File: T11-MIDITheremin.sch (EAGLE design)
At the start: 102 parts, among them IC1 TL072P, IC2 TL072P, T1 2N3904, T2 2N3904, T3 2N3904, T4 2N3904, T5 2N3904

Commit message: Add files via upload
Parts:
- removed L4, L5, L6: 10mH, rcl:L-US6000-XXX-RC
- added C32: 2200pF, resistor:C-EU050-025X075
- C2, C4: value 3n3 .1% -> 1.2nF
- L1: value 100uH .1% -> 2.5mH; device rcl:L-US6000-XXX-RC -> resistor:L-US0207/5V
- L2: value 100uH .1% -> 100uH; device rcl:L-US6000-XXX-RC -> resistor:L-US0207/5V
- L3: value 10mH -> 100uH; device rcl:L-US6000-XXX-RC -> resistor:L-US0207/5V
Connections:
- removed net ANT: ANT1.1, L6.2
- removed net N$19: L5.1, L6.1
- removed net N$35: L4.2, L5.2
- net N$20: now also C32.1
- net N$28: now also ANT1.1, L1.1; no longer L3.1, L4.1
- net P_OSC_V+: now also L3.1; no longer L1.1
- net V-: now also C32.2
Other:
- moved on the sheet: ANT1, C27, L1, L3, R32, VOUT

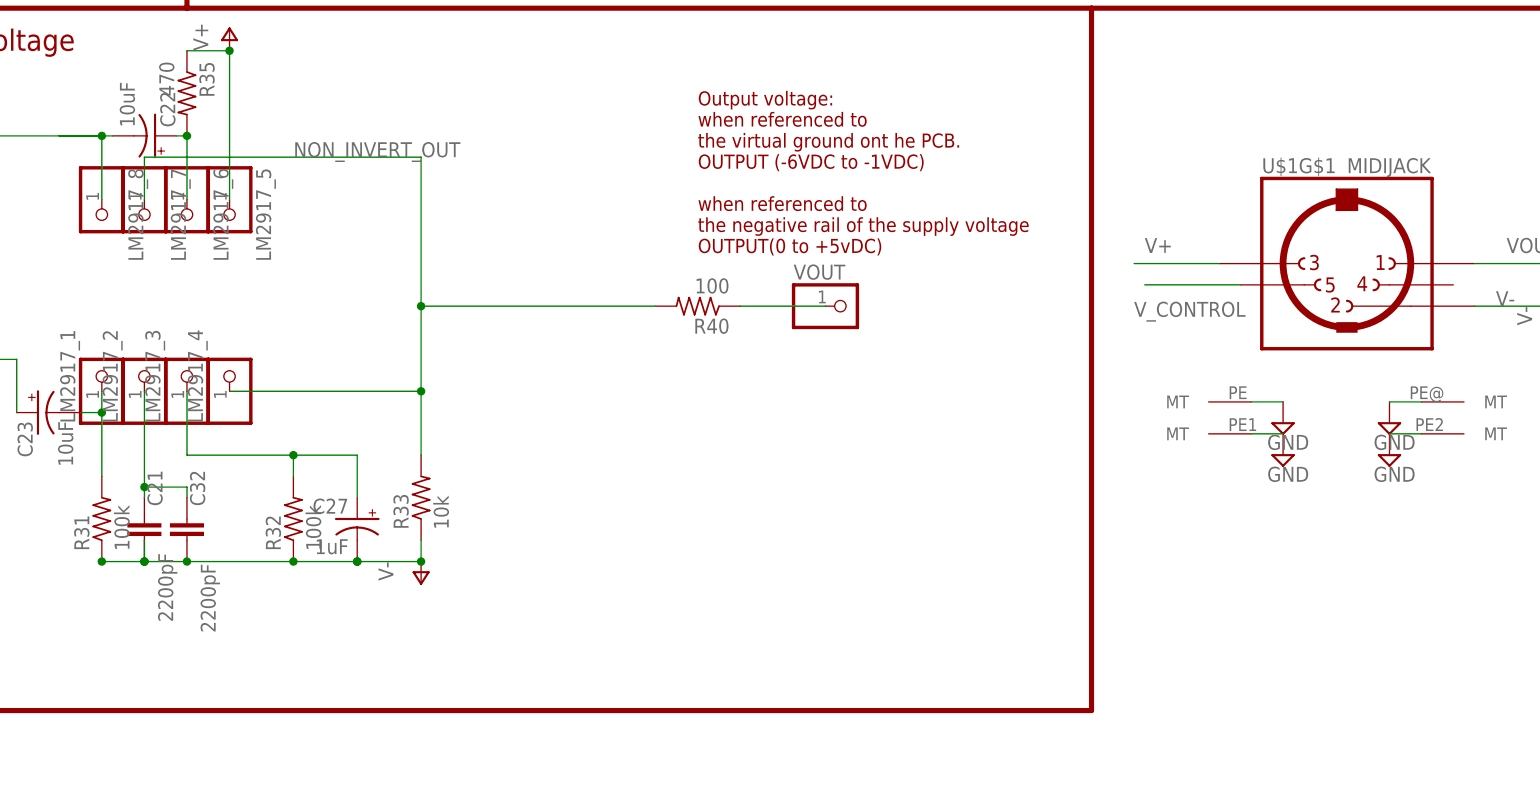
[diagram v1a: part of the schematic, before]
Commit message: fixed some of the silkscreen layer
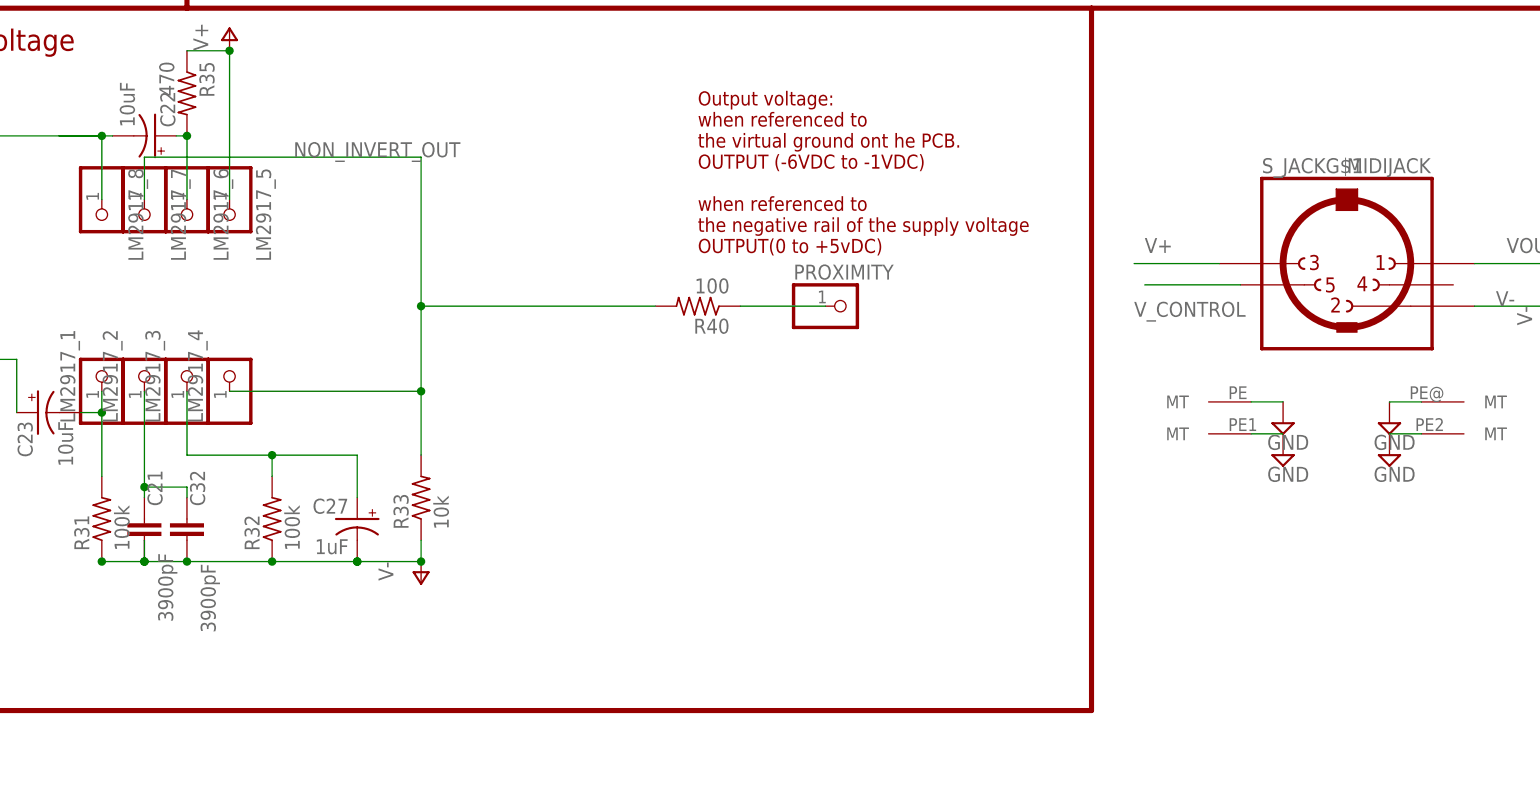
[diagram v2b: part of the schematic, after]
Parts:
- C21, C32: value 2200pF -> 3900pF
- renumbered U$1 to S_JACK, VOUT to PROXIMITY
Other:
- moved on the sheet: R32
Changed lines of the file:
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@@
 <setting verticaltext="up"/>
 </settings>
-<grid distance="0.05" unitdist="inch" unit="inch" style="lines" multiple="1" display="no" altdistance="0.01" altunitdist="inch" altunit="inch"/>
+<grid distance="0.1" unitdist="inch" unit="inch" style="lines" multiple="1" display="no" altdistance="0.01" altunitdist="inch" altunit="inch"/>
 <layers>
 <layer number="1" name="Top" color="4" fill="1" visible="no" active="no"/>
@@
 <part name="P+3" library="supply1" deviceset="V+" device=""/>
 <part name="P-2" library="supply1" deviceset="V-" device=""/>
-<part name="C21" library="resistor" deviceset="C-EU" device="050-025X075" value="2200pF"/>
+<part name="C21" library="resistor" deviceset="C-EU" device="050-025X075" value="3900pF"/>
 <part name="R31" library="rcl" deviceset="R-US_" device="0411/3V" value="100k"/>
 <part name="R32" library="rcl" deviceset="R-US_" device="0411/3V" value="100k"/>
@@
 <part name="LM2917_7" library="pinhead" deviceset="PINHD-1X1" device=""/>
 <part name="LM2917_8" library="pinhead" deviceset="PINHD-1X1" device=""/>
-<part name="VOUT" library="pinhead" deviceset="PINHD-1X1" device=""/>
+<part name="PROXIMITY" library="pinhead" deviceset="PINHD-1X1" device=""/>
 <part name="C27" library="resistor" deviceset="CPOL-US" device="E2.5-7" value="1uF"/>
 <part name="C23" library="resistor" deviceset="CPOL-US" device="E2.5-7" value="10uF"/>
@@
 <part name="C30" library="resistor" deviceset="C-EU" device="050-025X075" value="tune"/>
 <part name="C31" library="resistor" deviceset="C-EU" device="050-025X075" value="tune"/>
-<part name="U$1" library="adafruit" deviceset="MIDIJACK" device=""/>
+<part name="S_JACK" library="adafruit" deviceset="MIDIJACK" device=""/>
 <part name="P-1" library="supply1" deviceset="V-" device=""/>
 <part name="SUPPLY22" library="supply2" deviceset="GND" device=""/>
@@
 <part name="SUPPLY24" library="supply2" deviceset="GND" device=""/>
 <part name="SUPPLY25" library="supply2" deviceset="GND" device=""/>
-<part name="C32" library="resistor" deviceset="C-EU" device="050-025X075" value="2200pF"/>
+<part name="C32" library="resistor" deviceset="C-EU" device="050-025X075" value="3900pF"/>
 <part name="L3" library="resistor" deviceset="L-US" device="0207/5V" value="100uH"/>
 <part name="L1" library="resistor" deviceset="L-US" device="0207/5V" value="2.5mH"/>
@@
 </instance>
 <instance part="R31" gate="G$1" x="208.28" y="106.68" rot="R90"/>
-<instance part="R32" gate="G$1" x="231.14" y="106.68" rot="R90"/>
+<instance part="R32" gate="G$1" x="228.6" y="106.68" rot="R90"/>
 <instance part="R33" gate="G$1" x="246.38" y="109.22" rot="R90"/>
 <instance part="R35" gate="G$1" x="218.44" y="157.48" rot="R270"/>
@@
 <instance part="LM2917_7" gate="G$1" x="213.36" y="142.24" rot="R270"/>
 <instance part="LM2917_8" gate="G$1" x="208.28" y="142.24" rot="R270"/>
-<instance part="VOUT" gate="G$1" x="297.18" y="132.08"/>
+<instance part="PROXIMITY" gate="G$1" x="297.18" y="132.08"/>
 <instance part="C27" gate="G$1" x="238.76" y="106.68" rot="MR0"/>
 <instance part="C23" gate="G$1" x="200.66" y="119.38" rot="MR270"/>
@@
 <instance part="C30" gate="G$1" x="85.09" y="209.55"/>
 <instance part="C31" gate="G$1" x="78.74" y="215.9"/>
-<instance part="U$1" gate="G$1" x="356.87" y="137.16"/>
+<instance part="S_JACK" gate="G$1" x="356.87" y="137.16"/>
 <instance part="P-1" gate="1" x="382.27" y="129.54"/>
-<instance part="U$1" gate="G$2" x="345.44" y="120.65" rot="R180"/>
-<instance part="U$1" gate="G$3" x="365.76" y="120.65"/>
-<instance part="U$1" gate="G$4" x="345.44" y="116.84" rot="R180"/>
-<instance part="U$1" gate="G$5" x="365.76" y="116.84"/>
+<instance part="S_JACK" gate="G$2" x="345.44" y="120.65" rot="R180"/>
+<instance part="S_JACK" gate="G$3" x="365.76" y="120.65"/>
+<instance part="S_JACK" gate="G$4" x="345.44" y="116.84" rot="R180"/>
+<instance part="S_JACK" gate="G$5" x="365.76" y="116.84"/>
 <instance part="SUPPLY22" gate="GND" x="361.95" y="114.3"/>
 <instance part="SUPPLY23" gate="GND" x="349.25" y="114.3"/>
@@
 </segment>
 <segment>
-<pinref part="U$1" gate="G$1" pin="3"/>
+<pinref part="S_JACK" gate="G$1" pin="3"/>
 <wire x1="341.63" y1="137.16" x2="331.47" y2="137.16" width="0.1524" layer="91"/>
 <label x="332.74" y="138.43" size="1.778" layer="95"/>
@@
 <pinref part="R32" gate="G$1" pin="1"/>
 <wire x1="208.28" y1="101.6" x2="213.36" y2="101.6" width="0.1524" layer="91"/>
-<wire x1="231.14" y1="101.6" x2="218.44" y2="101.6" width="0.1524" layer="91"/>
+<wire x1="228.6" y1="101.6" x2="218.44" y2="101.6" width="0.1524" layer="91"/>
 <junction x="213.36" y="101.6"/>
 <junction x="208.28" y="101.6"/>
-<junction x="231.14" y="101.6"/>
+<junction x="228.6" y="101.6"/>
 <wire x1="218.44" y1="101.6" x2="213.36" y2="101.6" width="0.1524" layer="91"/>
 <wire x1="213.36" y1="101.6" x2="213.36" y2="104.14" width="0.1524" layer="91"/>
-<wire x1="231.14" y1="101.6" x2="238.76" y2="101.6" width="0.1524" layer="91"/>
+<wire x1="228.6" y1="101.6" x2="238.76" y2="101.6" width="0.1524" layer="91"/>
 <junction x="238.76" y="101.6"/>
 <wire x1="238.76" y1="101.6" x2="246.38" y2="101.6" width="0.1524" layer="91"/>
@@
 </segment>
 <segment>
-<pinref part="U$1" gate="G$1" pin="2"/>
+<pinref part="S_JACK" gate="G$1" pin="2"/>
 <wire x1="372.11" y1="132.08" x2="382.27" y2="132.08" width="0.1524" layer="91"/>
 <pinref part="P-1" gate="1" pin="V-"/>
@@
 </segment>
 <segment>
-<pinref part="U$1" gate="G$2" pin="MT"/>
+<pinref part="S_JACK" gate="G$2" pin="MT"/>
 <pinref part="SUPPLY24" gate="GND" pin="GND"/>
 <wire x1="345.44" y1="120.65" x2="349.25" y2="120.65" width="0.1524" layer="91"/>
 </segment>
 <segment>
-<pinref part="U$1" gate="G$4" pin="MT"/>
+<pinref part="S_JACK" gate="G$4" pin="MT"/>
 <pinref part="SUPPLY23" gate="GND" pin="GND"/>
 <wire x1="345.44" y1="116.84" x2="349.25" y2="116.84" width="0.1524" layer="91"/>
 </segment>
 <segment>
-<pinref part="U$1" gate="G$3" pin="MT"/>
+<pinref part="S_JACK" gate="G$3" pin="MT"/>
 <pinref part="SUPPLY25" gate="GND" pin="GND"/>
 <wire x1="365.76" y1="120.65" x2="361.95" y2="120.65" width="0.1524" layer="91"/>
 </segment>
 <segment>
-<pinref part="U$1" gate="G$5" pin="MT"/>
+<pinref part="S_JACK" gate="G$5" pin="MT"/>
 <pinref part="SUPPLY22" gate="GND" pin="GND"/>
 <wire x1="365.76" y1="116.84" x2="361.95" y2="116.84" width="0.1524" layer="91"/>
@@
 </segment>
 <segment>
-<pinref part="U$1" gate="G$1" pin="5"/>
+<pinref part="S_JACK" gate="G$1" pin="5"/>
 <wire x1="344.17" y1="134.62" x2="332.74" y2="134.62" width="0.1524" layer="91"/>
 <label x="331.47" y="130.81" size="1.778" layer="95"/>
@@
 <segment>
 <wire x1="218.44" y1="121.92" x2="218.44" y2="114.3" width="0.1524" layer="91"/>
-<wire x1="218.44" y1="114.3" x2="231.14" y2="114.3" width="0.1524" layer="91"/>
-<wire x1="231.14" y1="114.3" x2="238.76" y2="114.3" width="0.1524" layer="91"/>
+<wire x1="218.44" y1="114.3" x2="228.6" y2="114.3" width="0.1524" layer="91"/>
+<wire x1="228.6" y1="114.3" x2="238.76" y2="114.3" width="0.1524" layer="91"/>
 <pinref part="R32" gate="G$1" pin="2"/>
-<wire x1="231.14" y1="111.76" x2="231.14" y2="114.3" width="0.1524" layer="91"/>
-<junction x="231.14" y="114.3"/>
+<wire x1="228.6" y1="111.76" x2="228.6" y2="114.3" width="0.1524" layer="91"/>
+<junction x="228.6" y="114.3"/>
 <pinref part="LM2917_3" gate="G$1" pin="1"/>
 <pinref part="C27" gate="G$1" pin="+"/>
@@
 <net name="VOUT" class="0">
 <segment>
-<pinref part="VOUT" gate="G$1" pin="1"/>
+<pinref part="PROXIMITY" gate="G$1" pin="1"/>
 <pinref part="R40" gate="G$1" pin="1"/>
 <wire x1="284.48" y1="132.08" x2="294.64" y2="132.08" width="0.1524" layer="91"/>
 </segment>
 <segment>
-<pinref part="U$1" gate="G$1" pin="1"/>
+<pinref part="S_JACK" gate="G$1" pin="1"/>
 <wire x1="372.11" y1="137.16" x2="382.27" y2="137.16" width="0.1524" layer="91"/>
 <label x="375.92" y="138.43" size="1.778" layer="95"/>
